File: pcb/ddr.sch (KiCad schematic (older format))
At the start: 30 parts, among them U100 MCIMX7S5EVM08SC, U200 IS43LD32640B

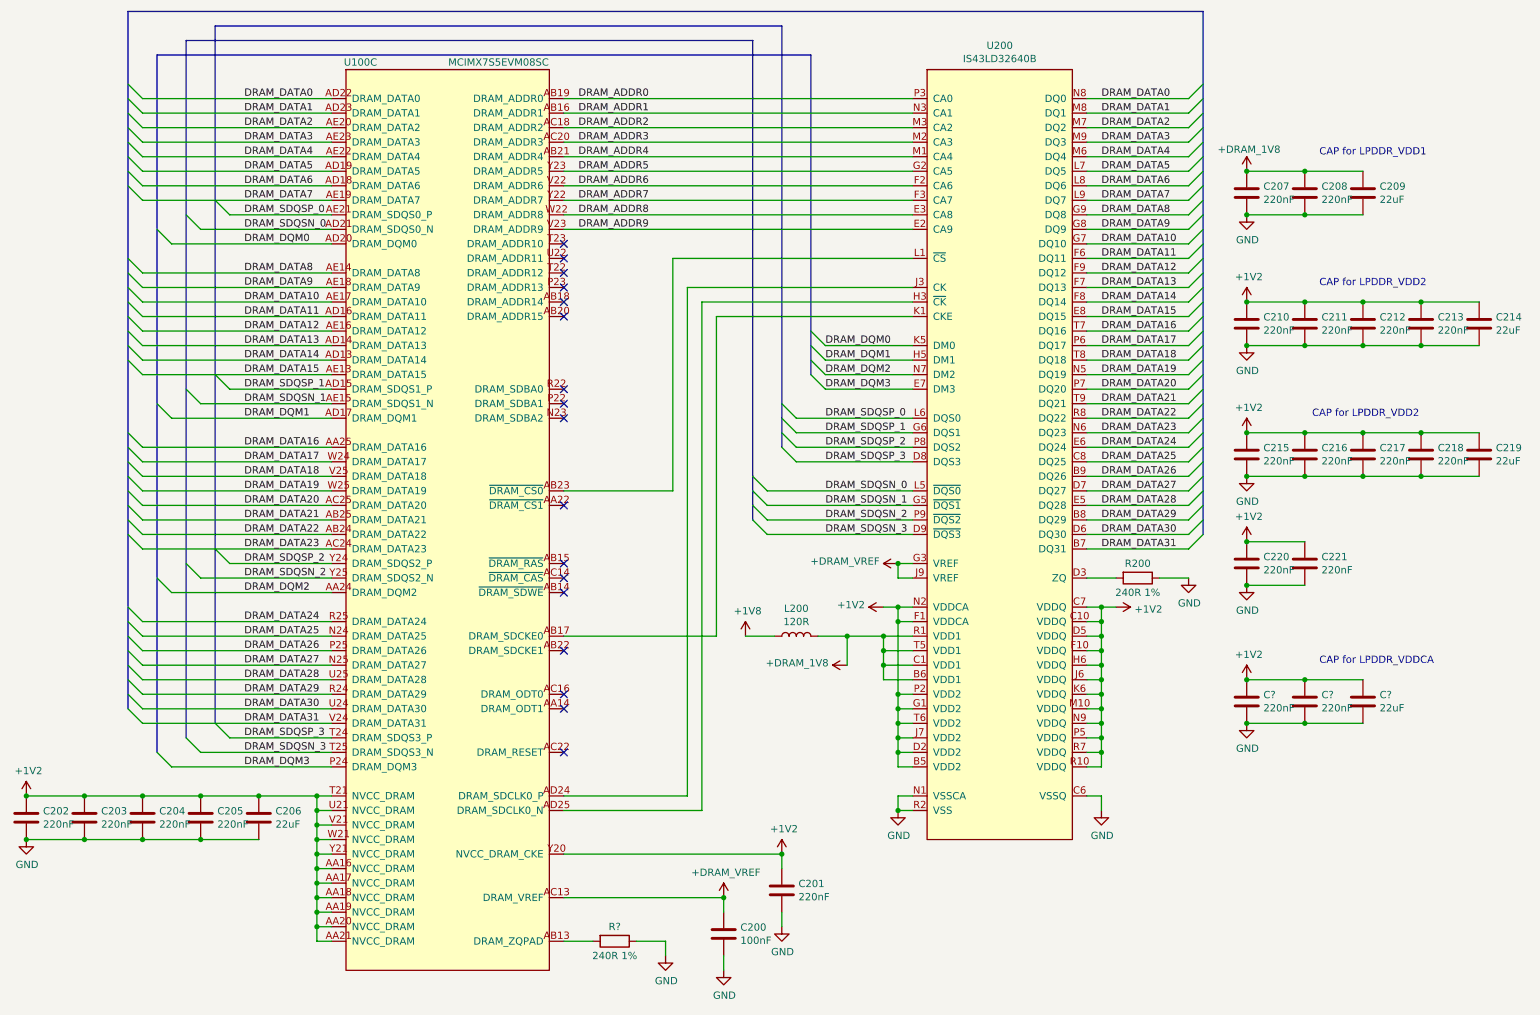
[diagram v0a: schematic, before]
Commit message: pcb: working on storage sch
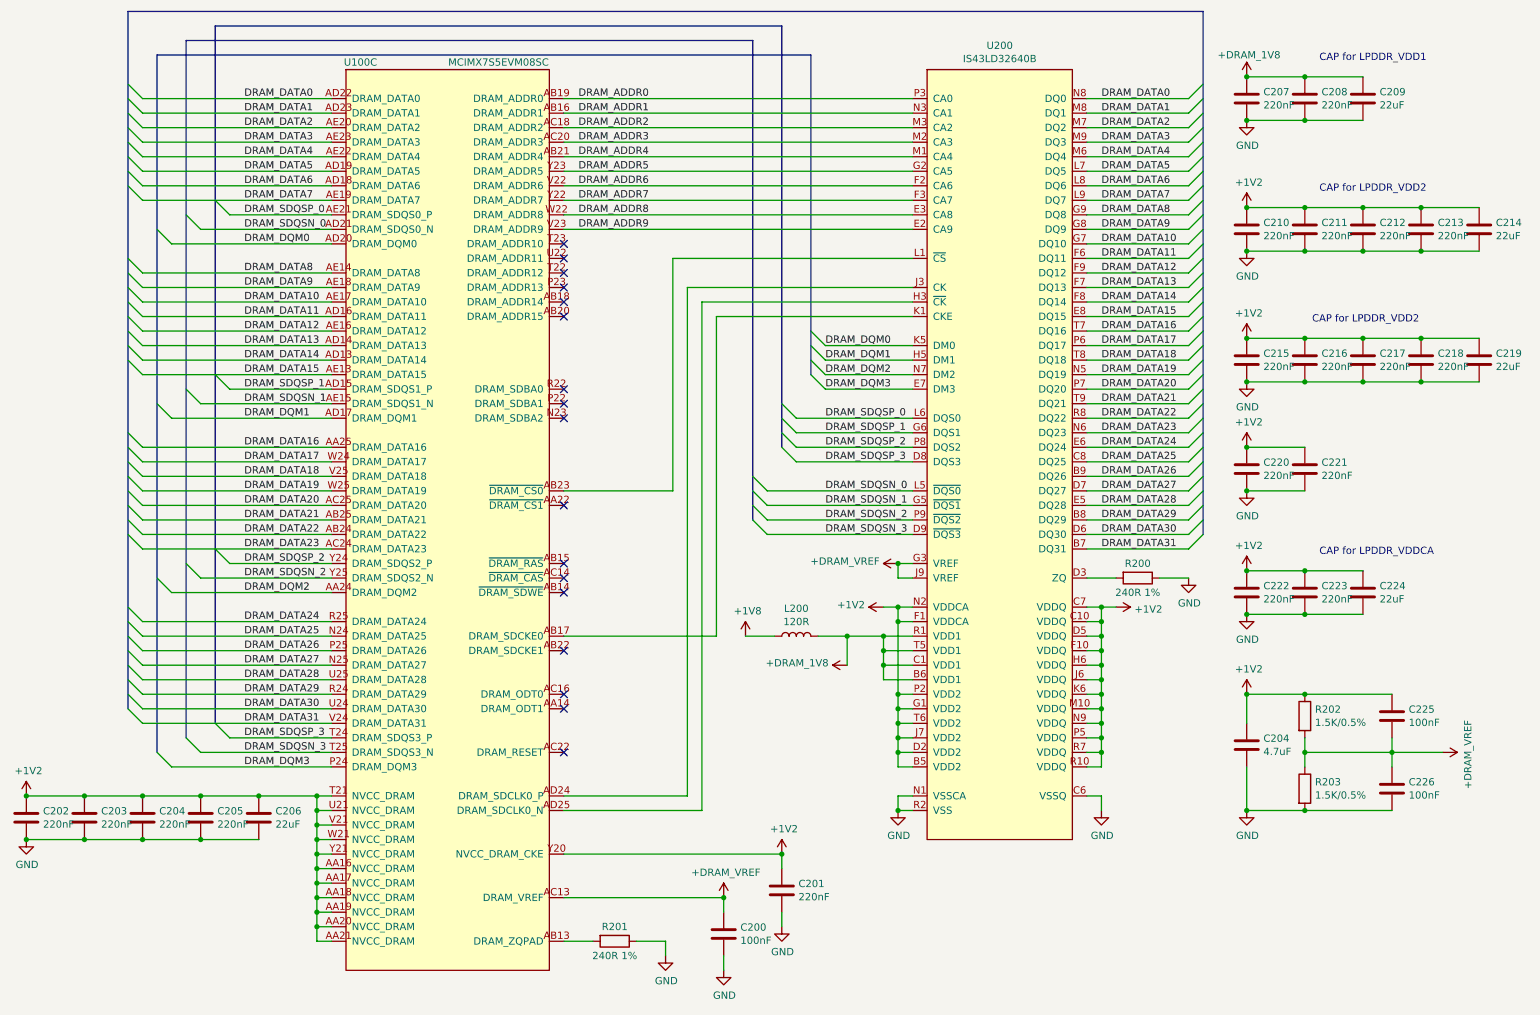
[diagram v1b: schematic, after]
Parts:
- added C204: 4.7uF, symbol Device:C
- added C225, C226: 100nF, symbol Device:C
- added R202, R203: 1.5K/0.5%, symbol Device:R
- gave numbers to parts that had none: 4
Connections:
- net +1V2: now also C204.1, C225.1, R202.1
- net +DRAM_VREF: now also C225.2, C226.1, R202.2, R203.1
- net GND: now also C204.2, C226.2, R203.2
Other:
- moved on the sheet: C207, C208, C209, C210, C211, C212, C213, C214, C215, C216, C217, C218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

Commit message: pcb: working on sch
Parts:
- added R204: 10K, symbol Device:R
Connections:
- net GND: now also R204.2
- net at U100.AB17 (DRAM_SDCKE0), U200.K1 (CKE): now also R204.1
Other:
- note added: "For LPDDR2,\nDRAM_RESET should be left unconnected\n"
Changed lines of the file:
@@
 $Descr A4 11693 8268
 encoding utf-8
-Sheet 4 7
+Sheet 4 10
 Title "LPDDR2 SDRAM"
 Date ""
@@
 	5450 2700 6900 2700
 Wire Wire Line
-	4500 5000 5550 5000
+	4500 5000 4950 5000
 Wire Wire Line
 	5550 5000 5550 2800
@@
 Wire Wire Line
 	10550 5800 10200 5800
+Text Notes 4650 5800 0    50   ~ 0
+For LPDDR2,\nDRAM_RESET should be left unconnected\n
+$Comp
+L Device:R R204
+U 1 1 5D1B9D3D
+P 4950 5250
+F 0 "R204" H 5020 5296 50  0000 L CNN
+F 1 "10K" H 5020 5205 50  0000 L CNN
+F 2 "" V 4880 5250 50  0001 C CNN
+F 3 "~" H 4950 5250 50  0001 C CNN
+	1    4950 5250
+	1    0    0    -1
+$EndComp
+Wire Wire Line
+	4950 5100 4950 5000
+Connection ~ 4950 5000
+Wire Wire Line
+	4950 5000 5550 5000
+$Comp
+L power:GND #PWR?
+U 1 1 5D1D2EB6
+P 4950 5400
+F 0 "#PWR?" H 4950 5150 50  0001 C CNN
+F 1 "GND" H 4955 5227 50  0000 C CNN
+F 2 "" H 4950 5400 50  0001 C CNN
+F 3 "" H 4950 5400 50  0001 C CNN
+	1    4950 5400
+	1    0    0    -1
+$EndComp
 Wire Wire Line
 	1600 2000 2900 2000

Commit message: pcb: finishing sch for r0.1
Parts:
- C200, C201, C202, C203, C204, C205, C207, C208, C210, C211, C212, C213, C215, C216, C217, C218, C220, C221, C222, C223, C225, C226: footprint (none) -> Capacitor_SMD:C_0402_1005Metric
- C204, C206, C209, C214, C219, C224: footprint (none) -> Capacitor_SMD:C_0603_1608Metric
- L200: footprint (none) -> Inductor_SMD:L_0603_1608Metric
- R200, R201, R202, R203, R204: footprint (none) -> Resistor_SMD:R_0603_1608Metric
- U100: footprint (none) -> footprints:BGA-541_25x25_19.0x19.0mm
- U200: footprint (none) -> footprints:BGA-134_10x17_10.0x11.5mm
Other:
- note added: "CAP for VDDQ"

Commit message: pcb: initial netlist
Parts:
- renumbered C204 to C227
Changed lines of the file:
@@
 Connection ~ 9200 4550
 $Comp
-L Device:C C204
+L Device:C C227
 U 1 1 5DBFDA85
 P 9200 5750
-F 0 "C204" H 9315 5796 50  0000 L CNN
+F 0 "C227" H 9315 5796 50  0000 L CNN
 F 1 "4.7uF" H 9315 5705 50  0000 L CNN
 F 2 "Capacitor_SMD:C_0603_1608Metric" H 9238 5600 50  0001 C CNN

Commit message: pcb: working on ddr
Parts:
- removed U200: IS43LD32640B, footprints:BGA-134_10x17_10.0x11.5mm, symbol symbols:IS43LD32640B
- added U200: IS43LD16128B, footprints:BGA-134_10x17_10.0x11.5mm, symbol symbols:IS43LD16128B
- R200, R201, R202, R203, R204: footprint Resistor_SMD:R_0603_1608Metric -> Resistor_SMD:R_0402_1005Metric
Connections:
- net +1V2: now also U200.B5 (VDD2), U200.C10 (VDDQ), U200.C7 (VDDQ), U200.D2 (VDD2), U200.D5 (VDDQ), U200.F1 (VDDCA), U200.F10 (VDDQ), U200.G1 (VDD2), U200.H6 (VDDQ), U200.J6 (VDDQ), U200.J7 (VDD2), U200.K6 (VDDQ), U200.M10 (VDDQ), U200.N2 (VDDCA), U200.N9 (VDDQ), U200.P2 (VDD2), U200.P5 (VDDQ), U200.R10 (VDDQ), U200.R7 (VDDQ), U200.T6 (VDD2)
- net +DRAM_1V8: now also U200.B6 (VDD1), U200.C1 (VDD1), U200.R1 (VDD1), U200.T5 (VDD1)
- net +DRAM_VREF: now also U200.G3 (VREF), U200.J9 (VREF)
- net DRAM_ADDR0: now also U200.P3 (CA0)
- net DRAM_ADDR1: now also U200.N3 (CA1)
- net DRAM_ADDR2: now also U200.M3 (CA2)
- net DRAM_ADDR3: now also U200.M2 (CA3)
- net DRAM_ADDR4: now also U200.M1 (CA4)
- net DRAM_ADDR5: now also U200.G2 (CA5)
- net DRAM_ADDR6: now also U200.F2 (CA6)
- net DRAM_ADDR7: now also U200.F3 (CA7)
- net DRAM_ADDR8: now also U200.E3 (CA8)
- net DRAM_ADDR9: now also U200.E2 (CA9)
- net DRAM_DATA0: now also U200.N8 (DQ0)
- net DRAM_DATA1: now also U200.M8 (DQ1)
- net DRAM_DATA10: now also U200.G7 (DQ10)
- net DRAM_DATA11: now also U200.F6 (DQ11)
- net DRAM_DATA12: now also U200.F9 (DQ12)
- net DRAM_DATA13: now also U200.F7 (DQ13)
- net DRAM_DATA14: now also U200.F8 (DQ14)
- net DRAM_DATA15: now also U200.E8 (DQ15)
- net DRAM_DATA2: now also U200.M7 (DQ2)
- net DRAM_DATA3: now also U200.M9 (DQ3)
- net DRAM_DATA4: now also U200.M6 (DQ4)
- net DRAM_DATA5: now also U200.L7 (DQ5)
- net DRAM_DATA6: now also U200.L8 (DQ6)
- net DRAM_DATA7: now also U200.L9 (DQ7)
- net DRAM_DATA8: now also U200.G9 (DQ8)
- net DRAM_DATA9: now also U200.G8 (DQ9)
- net DRAM_DQM0: now also U200.K5 (DM0)
- net DRAM_DQM1: now also U200.H5 (DM1)
- net DRAM_SDQSN_0: now also U200.L5 (~DQS0)
- net DRAM_SDQSN_1: now also U200.G5 (~DQS1)
- net DRAM_SDQSP_0: now also U200.L6 (DQS0)
- net DRAM_SDQSP_1: now also U200.G6 (DQS1)
- net GND: now also U200.C2 (VSS), U200.C5 (VSS), U200.C6 (VSSQ), U200.C9 (VSSQ), U200.D1 (VSS), U200.D10 (VSSQ), U200.E1 (VSSCA), U200.F5 (VSSQ), U200.G10 (VSSQ), U200.H2 (VSS), U200.J1 (VSSCA), U200.J5 (VSSQ), U200.J8 (VSS), U200.L10 (VSSQ), U200.M5 (VSSQ), U200.N1 (VSSCA), U200.N10 (VSSQ), U200.P1 (VSS), U200.P10 (VSSQ), U200.R2 (VSS), U200.R5 (VSS), U200.R6 (VSSQ), U200.R9 (VSSQ)
- net at R204.1, U100.AB17 (DRAM_SDCKE0): now also U200.K1 (CKE)
- net at U100.AB23 (~DRAM_CS0): now also U200.L1 (~CS)
- net at U100.AD24 (DRAM_SDCLK0_P): now also U200.J3 (CK)
- net at U100.AD25 (DRAM_SDCLK0_N): now also U200.H3 (~CK)
- net at R200.2: now also U200.D3 (ZQ)
- net DRAM_DATA16: no longer names the net of U100.AA25 (DRAM_DATA16)
- net DRAM_DATA17: no longer names the net of U100.W24 (DRAM_DATA17)
- net DRAM_DATA18: no longer names the net of U100.V25 (DRAM_DATA18)
- net DRAM_DATA19: no longer names the net of U100.W25 (DRAM_DATA19)
- net DRAM_DATA20: no longer names the net of U100.AC25 (DRAM_DATA20)
- net DRAM_DATA21: no longer names the net of U100.AB25 (DRAM_DATA21)
- net DRAM_DATA22: no longer names the net of U100.AB24 (DRAM_DATA22)
- net DRAM_DATA23: no longer names the net of U100.AC24 (DRAM_DATA23)
- net DRAM_DATA24: no longer names the net of U100.R25 (DRAM_DATA24)
- net DRAM_DATA25: no longer names the net of U100.N24 (DRAM_DATA25)
- net DRAM_DATA26: no longer names the net of U100.P25 (DRAM_DATA26)
- net DRAM_DATA27: no longer names the net of U100.N25 (DRAM_DATA27)
- net DRAM_DATA28: no longer names the net of U100.U25 (DRAM_DATA28)
- net DRAM_DATA29: no longer names the net of U100.R24 (DRAM_DATA29)
- net DRAM_DATA30: no longer names the net of U100.U24 (DRAM_DATA30)
- net DRAM_DATA31: no longer names the net of U100.V24 (DRAM_DATA31)
- net DRAM_DQM2: no longer names the net of U100.AA24 (DRAM_DQM2)
- net DRAM_DQM3: no longer names the net of U100.P24 (DRAM_DQM3)
- net DRAM_SDQSN_2: no longer names the net of U100.Y25 (DRAM_SDQS2_N)
- net DRAM_SDQSN_3: no longer names the net of U100.T25 (DRAM_SDQS3_N)
- net DRAM_SDQSP_2: no longer names the net of U100.Y24 (DRAM_SDQS2_P)
- net DRAM_SDQSP_3: no longer names the net of U100.T24 (DRAM_SDQS3_P)
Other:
- moved on the sheet: R204

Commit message: pcb: routing
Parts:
- C200, C201, C202, C203, C204, C205, C206, C207, C208, C209, C210, C211, C212, C213, C214, C215, C216, C217, C218, C219, C220, C221, C222, C223, C224, C225, C226, C227: symbol Device:C -> pcb-rescue:C-Device
- L200: symbol Device:L -> pcb-rescue:L-Device
- R200, R201, R202, R203, R204: symbol Device:R -> pcb-rescue:R-Device
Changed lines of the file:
@@
 NoConn ~ 4500 5800
 $Comp
-L power:+1V2 #PWR0171
+L pcb-rescue:+1V2-power #PWR0171
 U 1 1 5D6BF120
 P 6700 4800
@@
 $EndComp
 $Comp
-L power:+1V8 #PWR0173
+L pcb-rescue:+1V8-power #PWR0173
 U 1 1 5D70B95B
 P 5750 5000
@@
 	6700 5100 6700 5000
 $Comp
-L Device:L L200
+L pcb-rescue:L-Device L200
 U 1 1 5D753562
 P 6100 5000
@@
 	6450 5200 6450 5000
 $Comp
-L power:GND #PWR0175
+L pcb-rescue:GND-power #PWR0175
 U 1 1 5D774EFD
 P 6800 6200
@@
 $EndComp
 $Comp
-L power:GND #PWR0176
+L pcb-rescue:GND-power #PWR0176
 U 1 1 5D77587F
 P 8200 6200
@@
 $EndComp
 $Comp
-L power:+1V2 #PWR0177
+L pcb-rescue:+1V2-power #PWR0177
 U 1 1 5D77603C
 P 8300 4800
@@
 	8200 5800 8200 5700
 $Comp
-L Device:R R200
+L pcb-rescue:R-Device R200
 U 1 1 5D82DF01
 P 8450 4600
@@
 $EndComp
 $Comp
-L power:GND #PWR0178
+L pcb-rescue:GND-power #PWR0178
 U 1 1 5D82FD6C
 P 8800 4600
@@
 	8600 4600 8800 4600
 $Comp
-L Device:R R201
+L pcb-rescue:R-Device R201
 U 1 1 5D84AC72
 P 4850 7100
@@
 $EndComp
 $Comp
-L power:+1V2 #PWR0180
+L pcb-rescue:+1V2-power #PWR0180
 U 1 1 5D84C76E
 P 6000 6500
@@
 $EndComp
 $Comp
-L power:GND #PWR0181
+L pcb-rescue:GND-power #PWR0181
 U 1 1 5D84E07D
 P 5200 7200
@@
 $EndComp
 $Comp
-L Device:C C200
+L pcb-rescue:C-Device C200
 U 1 1 5D84EB60
 P 5600 7050
@@
 $EndComp
 $Comp
-L Device:C C201
+L pcb-rescue:C-Device C201
 U 1 1 5D84F753
 P 6000 6750
@@
 $EndComp
 $Comp
-L power:GND #PWR0182
+L pcb-rescue:GND-power #PWR0182
 U 1 1 5D8503EC
 P 5600 7300
@@
 $EndComp
 $Comp
-L power:GND #PWR0183
+L pcb-rescue:GND-power #PWR0183
 U 1 1 5D8505EC
 P 6000 7000
@@
 	4500 6800 5600 6800
 $Comp
-L Device:C C202
+L pcb-rescue:C-Device C202
 U 1 1 5D8EF254
 P 800 6250
@@
 $EndComp
 $Comp
-L Device:C C203
+L pcb-rescue:C-Device C203
 U 1 1 5D8F02C4
 P 1200 6250
@@
 $EndComp
 $Comp
-L Device:C C204
+L pcb-rescue:C-Device C204
 U 1 1 5D8F075C
 P 1600 6250
@@
 $EndComp
 $Comp
-L Device:C C205
+L pcb-rescue:C-Device C205
 U 1 1 5D8F0A94
 P 2000 6250
@@
 $EndComp
 $Comp
-L Device:C C206
+L pcb-rescue:C-Device C206
 U 1 1 5D946198
 P 2400 6250
@@
 $EndComp
 $Comp
-L power:+1V2 #PWR0184
+L pcb-rescue:+1V2-power #PWR0184
 U 1 1 5D947219
 P 800 6100
@@
 	2800 7000 2800 6900
 $Comp
-L power:GND #PWR0185
+L pcb-rescue:GND-power #PWR0185
 U 1 1 5DA15A1B
 P 800 6400
@@
 	2000 6400 1600 6400
 $Comp
-L Device:C C207
+L pcb-rescue:C-Device C207
 U 1 1 5DA309FE
 P 9200 1300
@@
 $EndComp
 $Comp
-L Device:C C208
+L pcb-rescue:C-Device C208
 U 1 1 5DA30A04
 P 9600 1300
@@
 $EndComp
 $Comp
-L Device:C C209
+L pcb-rescue:C-Device C209
 U 1 1 5DA30A16
 P 10000 1300
@@
 $EndComp
 $Comp
-L power:GND #PWR0186
+L pcb-rescue:GND-power #PWR0186
 U 1 1 5DA30A1C
 P 9200 1450
@@
 CAP for LPDDR_VDD2
 $Comp
-L Device:C C210
+L pcb-rescue:C-Device C210
 U 1 1 5DA70FA0
 P 9200 2200
@@
 $EndComp
 $Comp
-L Device:C C211
+L pcb-rescue:C-Device C211
 U 1 1 5DA70FA6
 P 9600 2200
@@
 $EndComp
 $Comp
-L Device:C C212
+L pcb-rescue:C-Device C212
 U 1 1 5DA70FAC
 P 10000 2200
@@
 $EndComp
 $Comp
-L Device:C C213
+L pcb-rescue:C-Device C213
 U 1 1 5DA70FB2
 P 10400 2200
@@
 $EndComp
 $Comp
-L Device:C C214
+L pcb-rescue:C-Device C214
 U 1 1 5DA70FB8
 P 10800 2200
@@
 $EndComp
 $Comp
-L power:GND #PWR0188
+L pcb-rescue:GND-power #PWR0188
 U 1 1 5DA70FBE
 P 9200 2350
@@
 	10400 2050 10000 2050
 $Comp
-L power:+1V2 #PWR0189
+L pcb-rescue:+1V2-power #PWR0189
 U 1 1 5DA86AA7
 P 9200 2050
@@
 Connection ~ 9200 2050
 $Comp
-L Device:C C215
+L pcb-rescue:C-Device C215
 U 1 1 5DA8B14B
 P 9200 3100
@@
 $EndComp
 $Comp
-L Device:C C216
+L pcb-rescue:C-Device C216
 U 1 1 5DA8B151
 P 9600 3100
@@
 $EndComp
 $Comp
-L Device:C C217
+L pcb-rescue:C-Device C217
 U 1 1 5DA8B157
 P 10000 3100
@@
 $EndComp
 $Comp
-L Device:C C218
+L pcb-rescue:C-Device C218
 U 1 1 5DA8B15D
 P 10400 3100
@@
 $EndComp
 $Comp
-L Device:C C219
+L pcb-rescue:C-Device C219
 U 1 1 5DA8B163
 P 10800 3100
@@
 $EndComp
 $Comp
-L power:GND #PWR0190
+L pcb-rescue:GND-power #PWR0190
 U 1 1 5DA8B169
 P 9200 3250
@@
 	10400 2950 10000 2950
 $Comp
-L power:+1V2 #PWR0191
+L pcb-rescue:+1V2-power #PWR0191
 U 1 1 5DA8B17E
 P 9200 2950
@@
 CAP for VDDQ
 $Comp
-L Device:C C220
+L pcb-rescue:C-Device C220
 U 1 1 5DAA272C
 P 9200 3850
@@
 $EndComp
 $Comp
-L Device:C C221
+L pcb-rescue:C-Device C221
 U 1 1 5DAA2732
 P 9600 3850
@@
 $EndComp
 $Comp
-L power:GND #PWR0192
+L pcb-rescue:GND-power #PWR0192
 U 1 1 5DAA2738
 P 9200 4000
@@
 	9600 4000 9200 4000
 $Comp
-L power:+1V2 #PWR0193
+L pcb-rescue:+1V2-power #PWR0193
 U 1 1 5DAA2744
 P 9200 3700
@@
 	9600 1450 10000 1450
 $Comp
-L Device:C C222
+L pcb-rescue:C-Device C222
 U 1 1 5DAD61D9
 P 9200 4700
@@
 $EndComp
 $Comp
-L Device:C C223
+L pcb-rescue:C-Device C223
 U 1 1 5DAD61DF
 P 9600 4700
@@
 $EndComp
 $Comp
-L Device:C C224
+L pcb-rescue:C-Device C224
 U 1 1 5DAD61E5
 P 10000 4700
@@
 $EndComp
 $Comp
-L power:GND #PWR0194
+L pcb-rescue:GND-power #PWR0194
 U 1 1 5DAD61EB
 P 9200 4850
@@
 	9600 4850 10000 4850
 $Comp
-L power:+1V2 #PWR0195
+L pcb-rescue:+1V2-power #PWR0195
 U 1 1 5DAEC398
 P 9200 4550
@@
 Connection ~ 9200 4550
 $Comp
-L Device:C C227
+L pcb-rescue:C-Device C227
 U 1 1 5DBFDA85
 P 9200 5750
@@
 $EndComp
 $Comp
-L Device:C C225
+L pcb-rescue:C-Device C225
 U 1 1 5DBFDE8B
 P 10200 5550
@@
 $EndComp
 $Comp
-L Device:C C226
+L pcb-rescue:C-Device C226
 U 1 1 5DBFE3CA
 P 10200 6050
@@
 $EndComp
 $Comp
-L Device:R R202
+L pcb-rescue:R-Device R202
 U 1 1 5DBFEB6C
 P 9600 5550
@@
 $EndComp
 $Comp
-L Device:R R203
+L pcb-rescue:R-Device R203
 U 1 1 5DBFF768
 P 9600 6050
@@
 $EndComp
 $Comp
-L power:GND #PWR0197
+L pcb-rescue:GND-power #PWR0197
 U 1 1 5DC70EC8
 P 9200 6200
@@
 $EndComp
 $Comp
-L power:+1V2 #PWR0198
+L pcb-rescue:+1V2-power #PWR0198
 U 1 1 5DC711F6
 P 9200 5400
@@
 For LPDDR2,\nDRAM_RESET should be left unconnected\n
 $Comp
-L Device:R R204
+L pcb-rescue:R-Device R204
 U 1 1 5D1B9D3D
 P 4900 5250
@@
 	4900 5100 4900 5000
 $Comp
-L power:GND #PWR0199
+L pcb-rescue:GND-power #PWR0199
 U 1 1 5D1D2EB6
 P 4900 5400
